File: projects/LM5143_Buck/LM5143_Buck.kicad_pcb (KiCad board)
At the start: 4 copper layers, 0 parts

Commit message: Placement
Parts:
- added C1: 4.7uF, Capacitor_SMD:C_1210_3225Metric, B.Cu at (127.8, 109.2)
- added C10: 2.2uF, Capacitor_SMD:C_0805_2012Metric, B.Cu at (144.5, 110.5)
- added C11: 10uF, Capacitor_SMD:C_1210_3225Metric, B.Cu at (124.2, 127.2)
- added C12: 100uF, Capacitor_THT:CP_Radial_D8.0mm_P3.50mm, F.Cu at (126.4, 130.2)
- added C13: 100uF, Capacitor_THT:CP_Radial_D8.0mm_P3.50mm, F.Cu at (153.6, 130.2)
- added C14: 10uF, Capacitor_SMD:C_1210_3225Metric, B.Cu at (155.8, 127.2)
- added C15: 100nF, Capacitor_SMD:C_0603_1608Metric, B.Cu at (135.0, 113.5)
- added C16: 100nF, Capacitor_SMD:C_0603_1608Metric, B.Cu at (145.0, 113.5)
- added C17: 3.3nF, Capacitor_SMD:C_0603_1608Metric, B.Cu at (145.5, 106.2)
- added C18: 82pF, Capacitor_SMD:C_0603_1608Metric, B.Cu at (145.5, 103.2)
- added C19: 100nF, Capacitor_SMD:C_0603_1608Metric, B.Cu at (145.5, 101.8)
- added C2: 4.7uF, Capacitor_SMD:C_1210_3225Metric, B.Cu at (131.2, 109.2)
- added C20: 470nF, Capacitor_SMD:C_0603_1608Metric, B.Cu at (137.5, 100.0)
- added C21: 470nF, Capacitor_SMD:C_0603_1608Metric, B.Cu at (139.2, 100.0)
- added C22: 10nF, Capacitor_SMD:C_0603_1608Metric, B.Cu at (142.8, 100.0)
- added C23: 1uF, Capacitor_SMD:C_0603_1608Metric, B.Cu at (150.8, 98.8)
- added C24: 1uF, Capacitor_SMD:C_0603_1608Metric, B.Cu at (144.8, 98.8)
- added C25: 100nF, Capacitor_SMD:C_0603_1608Metric, B.Cu at (130.2, 94.8)
- added C26: 1uF, Capacitor_SMD:C_0603_1608Metric, B.Cu at (132.8, 98.8)
- added C3: 4.7uF, Capacitor_SMD:C_1210_3225Metric, B.Cu at (148.8, 109.2)
- added C4: 4.7uF, Capacitor_SMD:C_1210_3225Metric, B.Cu at (152.2, 109.2)
- added C5: 330uF, Capacitor_THT:CP_Radial_D12.5mm_P5.00mm, F.Cu at (127.5, 89.8)
- added C6: 330uF, Capacitor_THT:CP_Radial_D12.5mm_P5.00mm, F.Cu at (141.0, 89.8)
- added C7: 330uF, Capacitor_THT:CP_Radial_D12.5mm_P5.00mm, F.Cu at (154.5, 89.8)
- added C8: 330uF, Capacitor_THT:CP_Radial_D12.5mm_P5.00mm, F.Cu at (168.0, 89.8)
- added C9: 2.2uF, Capacitor_SMD:C_0805_2012Metric, B.Cu at (135.5, 110.5)
- added D1: V2PM10L, Diode_SMD:D_SMP_DO-220AA, B.Cu at (138.2, 111.8)
- added D10: PLZ5V1C, footprints:D_MicroSMF, F.Cu at (137.8, 114.2)
- added D11: CUS10S30, Diode_SMD:D_SOD-323_HandSoldering, F.Cu at (147.0, 114.2)
- added D12: PLZ5V1C, footprints:D_MicroSMF, F.Cu at (142.2, 114.2)
- added D13: B18W1NG--20C000114U1930, LED_SMD:LED_0603_1608Metric, B.Cu at (134.5, 104.8)
- added D2: V2PM10L, Diode_SMD:D_SMP_DO-220AA, B.Cu at (141.8, 111.8)
- added D3: CUS10S30, Diode_SMD:D_SOD-323_HandSoldering, F.Cu at (133.0, 109.8)
- added D4: PLZ5V1C, footprints:D_MicroSMF, F.Cu at (137.8, 109.8)
- added D5: CUS10S30, Diode_SMD:D_SOD-323_HandSoldering, F.Cu at (147.0, 109.8)
- added D6: PLZ5V1C, footprints:D_MicroSMF, F.Cu at (142.2, 109.8)
- added D7: MBR15H120PC-AU, Package_TO_SOT_SMD:TO-277A, B.Cu at (129.8, 114.2)
- added D8: MBR15H120PC-AU, Package_TO_SOT_SMD:TO-277A, B.Cu at (150.2, 114.2)
- added D9: CUS10S30, Diode_SMD:D_SOD-323_HandSoldering, F.Cu at (133.0, 114.2)
- added J1: Bat In, footprints:XT60PW-F, F.Cu at (111.0, 84.5)
- added J2: 24V Out, footprints:XT60PW-F, F.Cu at (140.0, 135.5)
- added J3: I2C Socket, Connector_JST:JST_GH_SM04B-GHS-TB_1x04-1MP_P1.25mm_Horizontal, F.Cu at (178.2, 98.5)
- added J4: I2C Socket, Connector_JST:JST_GH_SM04B-GHS-TB_1x04-1MP_P1.25mm_Horizontal, F.Cu at (101.8, 98.5)
- added L1: 10uH, footprints:ER26A, F.Cu at (98.2, 117.5)
- added L2: 10uH, footprints:ER26A, F.Cu at (181.8, 117.5)
- added NT1: NetTie_2, footprints:NetTie-2_SMD_Pad0.25mm, B.Cu at (139.8, 103.2)
- added Q1: IGC025S08S1, footprints:PG‑TSON‑6, F.Cu at (129.2, 109.8)
- added Q2: IGC025S08S1, footprints:PG‑TSON‑6, F.Cu at (150.8, 109.8)
- added Q3: IGC025S08S1, footprints:PG‑TSON‑6, F.Cu at (129.2, 114.2)
- added Q4: IGC025S08S1, footprints:PG‑TSON‑6, F.Cu at (150.8, 114.2)
- added R1: 2.2, Resistor_SMD:R_0603_1608Metric, B.Cu at (136.2, 115.2)
- added R10: 2.2m, footprints:ASR2512, B.Cu at (151.0, 124.8)
- added R11: 3.3, Resistor_SMD:R_0603_1608Metric, F.Cu at (136.2, 114.5)
- added R12: 3.3, Resistor_SMD:R_0603_1608Metric, F.Cu at (143.8, 114.5)
- added R13: 10k, Resistor_SMD:R_0603_1608Metric, F.Cu at (139.2, 114.5)
- added R14: 10k, Resistor_SMD:R_0603_1608Metric, F.Cu at (140.8, 114.5)
- added R15: 1, Resistor_SMD:R_0603_1608Metric, F.Cu at (134.8, 114.5)
- added R16: 1, Resistor_SMD:R_0603_1608Metric, F.Cu at (145.2, 114.5)
- added R17: 3.3k, Resistor_SMD:R_0603_1608Metric, B.Cu at (134.5, 106.2)
- added R18: 100k, Resistor_SMD:R_0603_1608Metric, B.Cu at (141.0, 100.0)
- added R19: 18k, Resistor_SMD:R_0603_1608Metric, B.Cu at (145.5, 104.8)
- added R2: 2.2, Resistor_SMD:R_0603_1608Metric, B.Cu at (143.8, 115.2)
- added R20: 10k, Resistor_SMD:R_0603_1608Metric, B.Cu at (152.5, 98.8)
- added R21: 390k, Resistor_SMD:R_0603_1608Metric, B.Cu at (134.5, 101.8)
- added R22: 10k, Resistor_SMD:R_0603_1608Metric, B.Cu at (134.5, 103.2)
- added R23: 3.3k, Resistor_SMD:R_0603_1608Metric, B.Cu at (123.5, 97.0)
- added R24: 3.3k, Resistor_SMD:R_0603_1608Metric, B.Cu at (123.5, 95.2)
- added R25: 3.3k, Resistor_SMD:R_0603_1608Metric, B.Cu at (127.0, 94.8)
- added R26: 10, Resistor_SMD:R_0603_1608Metric, B.Cu at (130.2, 100.2)
- added R27, R30: 5m, footprints:PCSR2512_Alt, B.Cu at (140.0, 123.2)
- added R28: 5m, footprints:PCSR2512_Alt_2, B.Cu at (148.0, 123.2)
- added R29: 5m, footprints:PCSR2512_Alt_2, B.Cu at (144.0, 123.2)
- added R3: 3.3, Resistor_SMD:R_0603_1608Metric, F.Cu at (136.2, 109.5)
- added R31: 10, Resistor_SMD:R_0603_1608Metric, B.Cu at (134.5, 98.8)
- added R4: 3.3, Resistor_SMD:R_0603_1608Metric, F.Cu at (143.8, 109.5)
- added R5: 10k, Resistor_SMD:R_0603_1608Metric, F.Cu at (139.2, 109.5)
- added R6: 10k, Resistor_SMD:R_0603_1608Metric, F.Cu at (140.8, 109.5)
- added R7: 1, Resistor_SMD:R_0603_1608Metric, F.Cu at (134.8, 109.5)
- added R8: 1, Resistor_SMD:R_0603_1608Metric, F.Cu at (145.2, 109.5)
- added R9: 2.2m, footprints:ASR2512, B.Cu at (129.0, 124.8)
- added SW1: Addr_Switch, footprints:SLW-1478144-5A-S-D, F.Cu at (115.5, 99.0)
- added SW2: Addr_Switch, footprints:SLW-1478144-5A-S-D, F.Cu at (164.5, 99.0)
- added TP1: TestPoint, TestPoint:TestPoint_Keystone_5000-5004_Miniature, F.Cu at (100.8, 90.5)
- added TP2: TestPoint, TestPoint:TestPoint_Keystone_5000-5004_Miniature, F.Cu at (121.2, 90.5)
- added TP3: TestPoint, TestPoint:TestPoint_Keystone_5000-5004_Miniature, F.Cu at (123.8, 107.0)
- added TP4: TestPoint, TestPoint:TestPoint_Keystone_5000-5004_Miniature, F.Cu at (156.2, 106.8)
- added TP5: TestPoint, TestPoint:TestPoint_Keystone_5000-5004_Miniature, F.Cu at (150.2, 135.5)
- added TP6: TestPoint, TestPoint:TestPoint_Keystone_5000-5004_Miniature, F.Cu at (129.8, 135.5)
- added TP7: TestPoint, TestPoint:TestPoint_Pad_D2.0mm, B.Cu at (118.0, 96.0)
- added U1: ~, footprints:Texas_VQFN-40-1EP_6x6mm_P0.5mm_EP3.3x3.3mm_ThermalVias, B.Cu at (140.0, 105.5)
- added U2: TLV74033, Package_TO_SOT_SMD:SOT-23-5, B.Cu at (147.8, 98.8)
- added U3: INA226, Package_SO:VSSOP-10_3x3mm_P0.5mm, B.Cu at (128.5, 97.5)
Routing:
- net VOUT: track 0.00 -> 37.3 mm
- net +24V: track 0.00 -> 11.2 mm, vias 0 -> 55
- net PGND1: track 0.00 -> 8.78 mm
- net PGND2: track 0.00 -> 8.61 mm
- net Net-(D3-A): track 0.00 -> 8.61 mm
- net Net-(D3-K): track 0.00 -> 8.61 mm
- net Net-(D11-K): track 0.00 -> 8.61 mm
- net Net-(D5-A): track 0.00 -> 8.41 mm
- net Net-(D10-K): track 0.00 -> 7.99 mm
- net Net-(D5-K): track 0.00 -> 7.99 mm
- net Net-(U1-CS1): track 0.00 -> 4.98 mm
- net Net-(U1-CS2): track 0.00 -> 4.98 mm
- added copper zone on B.Cu, net +24V
- added copper zone on F.Cu, net +24V
- added copper zone on B.Cu, net GNDA
- added copper zone on B.Cu, net GNDPWR
- added copper zone on F.Cu, net GNDPWR
- added copper zone on In1.Cu, net GNDPWR
- added copper zone on In2.Cu, net GNDPWR
- added copper zone on B.Cu, net Net-(D7-K)
- added copper zone on F.Cu, net Net-(D7-K)
- added copper zone on B.Cu, net Net-(D8-K)
- added copper zone on F.Cu, net Net-(D8-K)
- added copper zone on B.Cu, net VDD
- added copper zone on F.Cu, net VDD
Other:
- board outline added: 83 x 55 mm
- board text added: "Heat Sink Area"

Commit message: PCB wiring
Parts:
- C17, R17, R19: moved to F.Cu
- moved SW2 49.1 mm to (164.5, 102.0), turned to 180 degrees
- moved SW1 49.0 mm to (115.5, 99.0)
- moved R19 3.01 mm to (145.8, 101.8)
- moved C17 2.24 mm to (146.5, 104.2), turned to 90 degrees
- moved D13 1.27 mm to (134.2, 106.0)
- moved R1 0.83 mm to (136.6, 116.0)
- moved R2 0.83 mm to (143.4, 116.0)
- moved D1 0.80 mm to (138.2, 112.6)
- moved D2 0.80 mm to (141.8, 112.6)
- moved D10 0.50 mm to (137.8, 114.8)
- moved D11 0.50 mm to (147.0, 114.8)
- moved D12 0.50 mm to (142.2, 114.8)
- moved D7 0.50 mm to (129.8, 114.8)
- moved D8 0.50 mm to (150.2, 114.8)
- moved D9 0.50 mm to (133.0, 114.8)
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- renumbered SW2 to SW1, SW1 to SW2
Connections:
- J1 pad : VDD -> GNDPWR
- J2 pad : +24V -> GNDPWR
- SW1 pad : VDD -> GNDPWR
- SW2 pad : VDD -> GNDPWR
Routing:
- net Net-(J3-Pin_3): track 0.00 -> 83.4 mm, vias 0 -> 1
- net Net-(J3-Pin_4): track 0.00 -> 82.8 mm, vias 0 -> 1
- net VOUT: track 37.3 -> 106.0 mm, vias 0 -> 6
- net +3.3V: track 0.00 -> 68.0 mm, vias 0 -> 2
- net +5V: track 0.00 -> 49.8 mm, vias 0 -> 3
- net +24V: track 11.2 -> 57.0 mm, vias 55 -> 57
- net GNDA: track 0.00 -> 45.2 mm, vias 0 -> 1
- net Net-(U3-A1): track 0.00 -> 40.0 mm, vias 0 -> 1
- net /~{Alert}: track 0.00 -> 34.9 mm, vias 0 -> 3
- net Net-(U1-CS1): track 4.98 -> 34.4 mm, vias 0 -> 2
- net Net-(U1-CS2): track 4.98 -> 33.7 mm, vias 0 -> 2
- net Net-(U1-COMP1): track 0.00 -> 15.9 mm, vias 0 -> 2
- net PGND2: track 8.61 -> 22.9 mm, vias 0 -> 2
- net Net-(U3-A0): track 0.00 -> 12.8 mm
- net Net-(U1-SS1): track 0.00 -> 11.4 mm, vias 0 -> 2
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- added copper zone on B.Cu, net VOUT

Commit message: Update stuff
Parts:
- removed the TP3 at (124.0, 107.0)
- removed the TP4 at (156.0, 107.0)
- moved J3 77.2 mm to (101.8, 88.0), turned to -90 degrees
- moved TP1 61.6 mm to (162.2, 86.8)
- moved J1 61.2 mm to (172.2, 84.5)
- moved TP2 58.3 mm to (179.2, 96.5)
- moved C5 16.2 mm to (111.2, 89.8)
- moved C6 16.2 mm to (124.8, 89.8)
- moved C7 16.2 mm to (138.2, 89.8)
- moved C8 16.2 mm to (151.8, 89.8)
- moved SW1 2.60 mm to (118.1, 99.0)
- moved SW2 2.60 mm to (161.9, 102.0)
- moved TP7 2.46 mm to (120.2, 97.0)
- renumbered TP5 to TP3, TP6 to TP4
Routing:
- net GNDA: track 45.2 -> 54.7 mm
- net +3.3V: track 68.0 -> 60.8 mm
- net Net-(J3-Pin_4): track 82.8 -> 78.1 mm, vias 1 -> 3
- net /~{Alert}: track 34.9 -> 32.3 mm
- net Net-(U3-A1): track 40.0 -> 37.4 mm
- net Net-(U3-A0): track 12.8 -> 10.2 mm
- net Net-(J3-Pin_3): track 83.4 -> 81.4 mm, vias 1 -> 3
- net VOUT: track 106.0 -> 103.9 mm
- net Net-(U1-CS1): track 34.4 -> 33.1 mm
- net Net-(U1-CS2): track 33.7 -> 32.9 mm
- net VDD: vias 21 -> 25
- net Net-(D8-K): vias 0 -> 10
- net Net-(D7-K): vias 0 -> 10
- net GNDPWR: vias 25 -> 175
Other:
- board text added: "+"
- board text added: "-"
- board text added: "24V"
- board text added: "BAT"
- board text added: "GND"
- board text added: "~{Alert}"

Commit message: minor fixes
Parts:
- moved TP1 2.25 mm to (162.2, 84.5)
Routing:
- net GNDPWR: vias 175 -> 176
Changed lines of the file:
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@@
 	(footprint "TestPoint:TestPoint_Keystone_5000-5004_Miniature"
 		(layer "F.Cu")
-		(at 162.25 86.75)
+		(at 162.25 84.5)
 		(descr "Keystone THM Miniature Test Point 5000-5004, http://www.keyelco.com/product-pdf.cfm?p=1309")
 		(tags "Through Hole Mount Test Points")
@@
 	)
 	(gr_text "BAT"
-		(at 162.25 84.25 0)
+		(at 159.25 83.75 0)
 		(layer "F.SilkS")
 		(effects
@@
 	)
 	(via
+		(at 162.5 87)
+		(size 0.6)
+		(drill 0.3)
+		(layers "F.Cu" "B.Cu")
+		(free yes)
+		(net 2)
+	)
+	(via
 		(at 162.5 114)
 		(size 0.6)
@@
 		(members "5062c024-5f6c-47a1-bfe0-1b14b4ad3ff2" "55c91df1-3d0a-4434-9000-f0a3faa70d4e")
 	)
-	(group ""
-		(members "0003389f-96c1-440a-82e1-2d7b16629ee7" "c15c7f08-a1d3-4b3f-ac85-2828c58cd0ea")
-	)
 	(embedded_fonts no)

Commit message: Minor changes
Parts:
- moved C17 1.25 mm to (145.8, 103.2), turned to 0 degrees
- renumbered TP7 to TP5
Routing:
- net GNDA: track 54.7 -> 55.8 mm

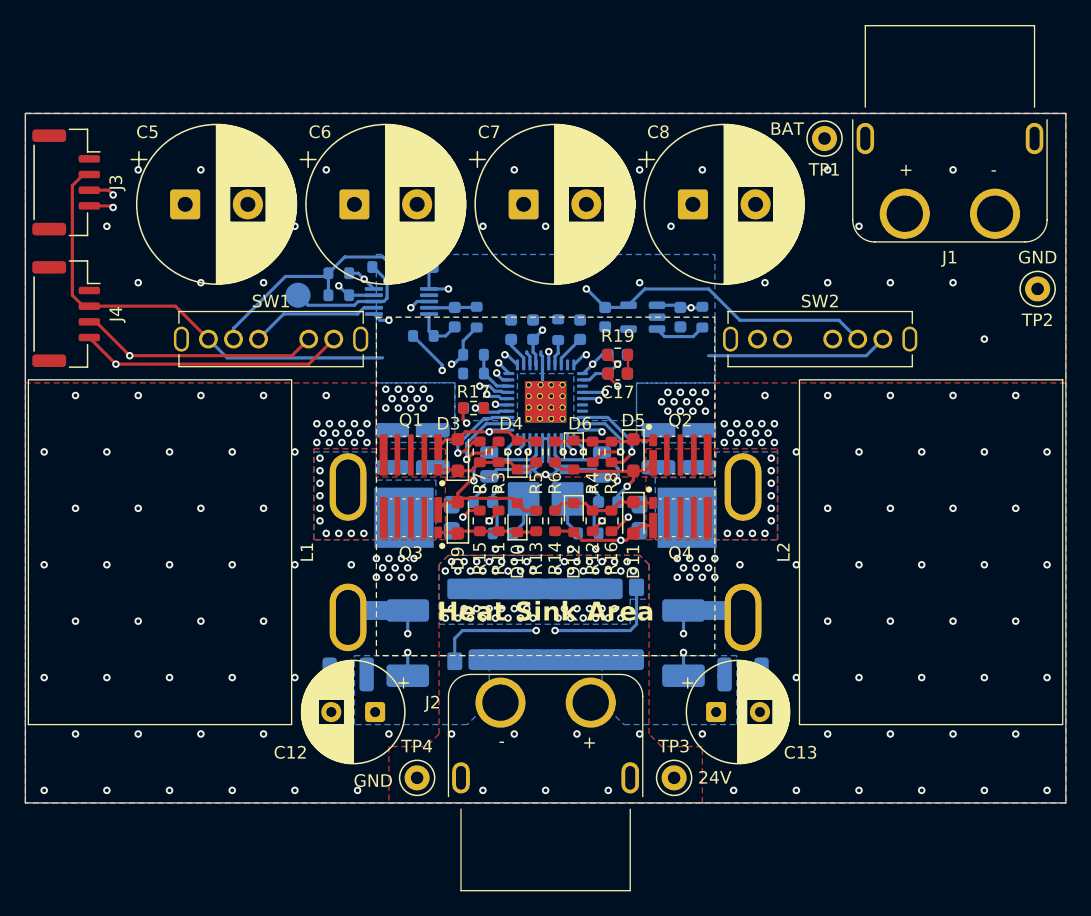
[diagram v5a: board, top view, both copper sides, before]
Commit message: Changed a few pad sizes
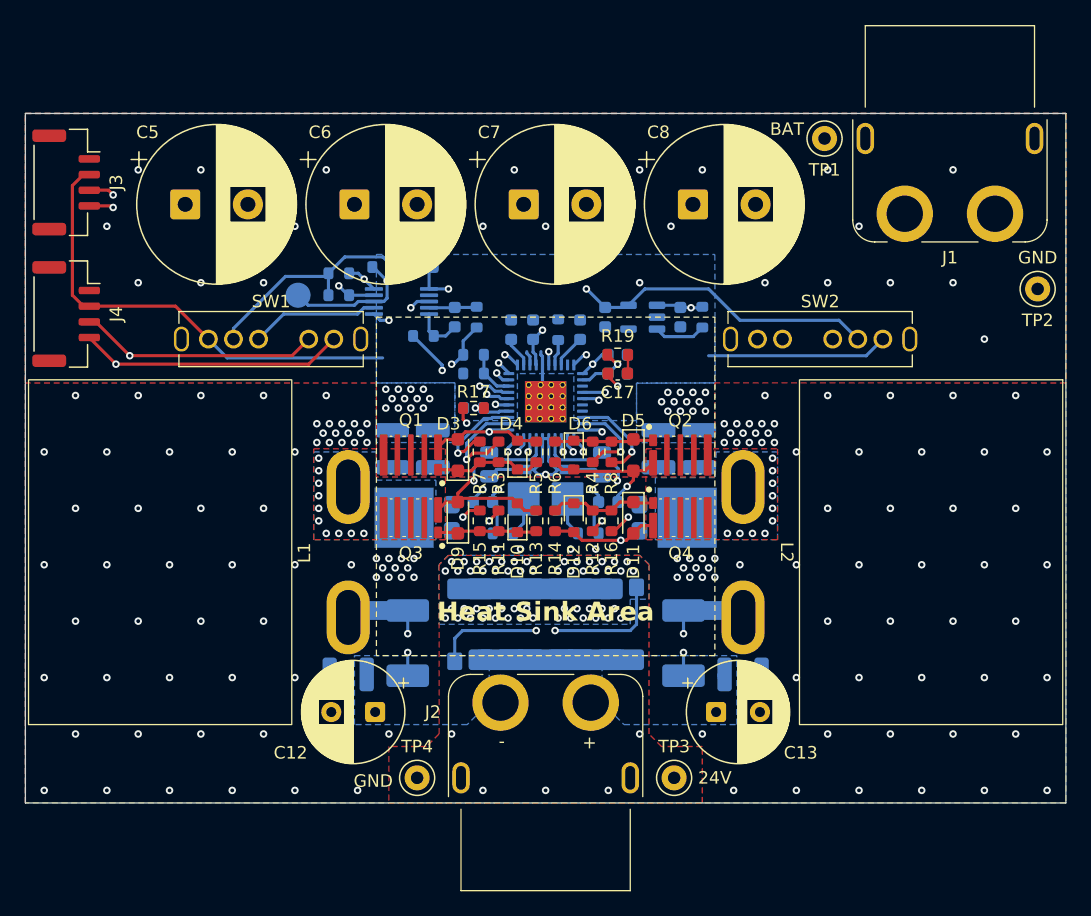
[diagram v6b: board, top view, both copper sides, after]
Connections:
- J3 pad MP: VDD -> (no net)
- J4 pad MP: VDD -> (no net)
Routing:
- net GNDPWR: vias 176 -> 174

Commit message: Change switch orientation, update XT60 name
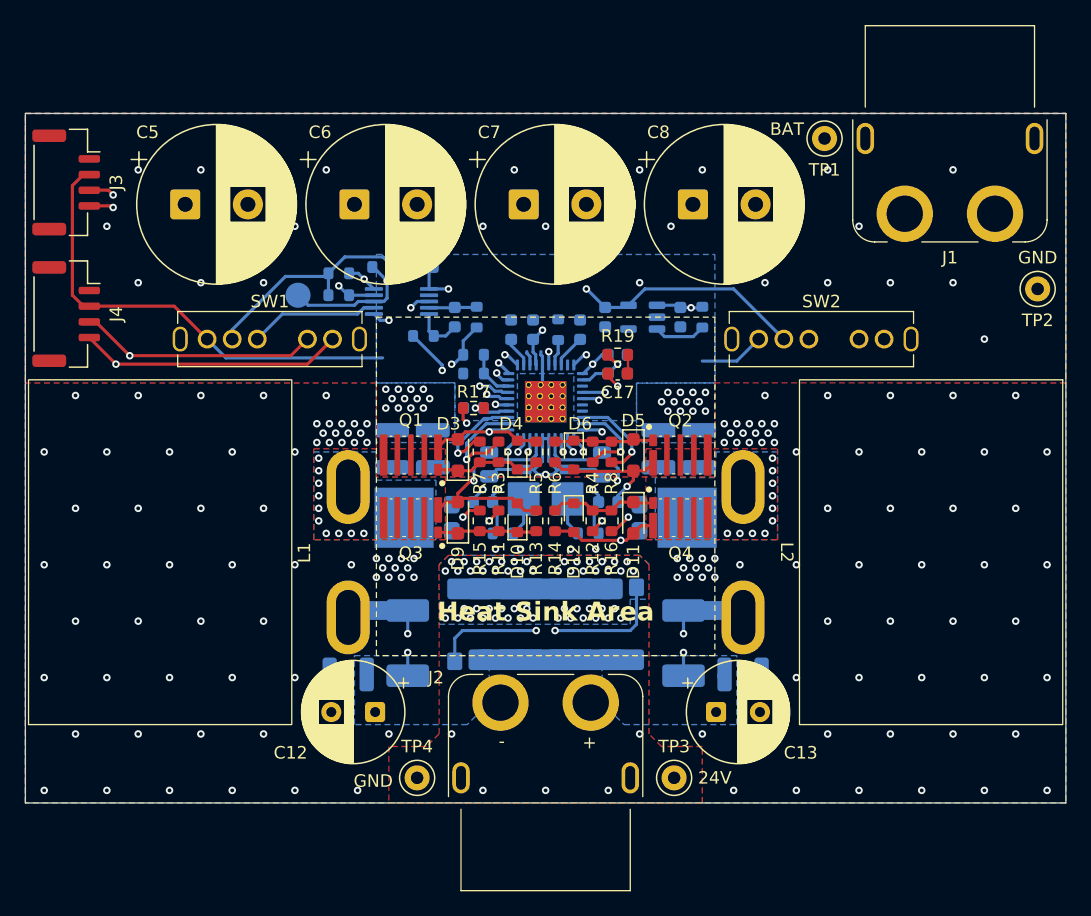
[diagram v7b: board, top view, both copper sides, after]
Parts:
- J1, J2: footprint footprints:XT60PW-F -> footprints:XT60PW
- moved SW2 3.00 mm to (162.0, 99.0), turned to 0 degrees
- moved SW1 0.10 mm to (118.0, 99.0)
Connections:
- SW1 pad : GNDPWR -> (no net)
- SW2 pad : GNDPWR -> (no net)
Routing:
- net Net-(J3-Pin_4): track 78.1 -> 88.7 mm
- net GNDA: track 55.8 -> 46.5 mm
- net Net-(J3-Pin_3): track 81.4 -> 87.4 mm
- net +3.3V: track 60.8 -> 55.0 mm
- net Net-(U3-A1): track 37.4 -> 35.5 mm

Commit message: Minor changes
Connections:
- J3 pad MP: (no net) -> VDD
- J4 pad MP: (no net) -> VDD
- SW1 pad : (no net) -> GNDPWR
- SW2 pad : (no net) -> GNDPWR
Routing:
- net GNDPWR: vias 174 -> 172
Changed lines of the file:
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@@
 			(layers "F.Cu" "F.Mask" "F.Paste")
 			(roundrect_rratio 0.25)
+			(net 1 "VDD")
 		)
 		(pad "MP" smd roundrect
@@
 			(layers "F.Cu" "F.Mask" "F.Paste")
 			(roundrect_rratio 0.25)
+			(net 1 "VDD")
 		)
 		(embedded_fonts no)
@@
 		(pad "" thru_hole oval
 			(at -7.15 1.5)
-			(size 1.2 2)
+			(size 1.4 2.2)
 			(drill oval 0.8 1.6)
 			(layers "*.Cu" "*.Mask")
 			(remove_unused_layers no)
+			(net 2 "GNDPWR")
 		)
 		(pad "" thru_hole oval
 			(at 7.15 1.5)
-			(size 1.2 2)
+			(size 1.4 2.2)
 			(drill oval 0.8 1.6)
 			(layers "*.Cu" "*.Mask")
 			(remove_unused_layers no)
+			(net 2 "GNDPWR")
 		)
 		(pad "1" thru_hole circle
@@
 			(layers "F.Cu" "F.Mask" "F.Paste")
 			(roundrect_rratio 0.25)
+			(net 1 "VDD")
 		)
 		(pad "MP" smd roundrect
@@
 			(layers "F.Cu" "F.Mask" "F.Paste")
 			(roundrect_rratio 0.25)
+			(net 1 "VDD")
 		)
 		(embedded_fonts no)
@@
 		(pad "" thru_hole oval
 			(at -7.15 1.5)
-			(size 1.2 2)
+			(size 1.4 2.2)
 			(drill oval 0.8 1.6)
 			(layers "*.Cu" "*.Mask")
 			(remove_unused_layers no)
+			(net 2 "GNDPWR")
 		)
 		(pad "" thru_hole oval
 			(at 7.15 1.5)
-			(size 1.2 2)
+			(size 1.4 2.2)
 			(drill oval 0.8 1.6)
 			(layers "*.Cu" "*.Mask")
 			(remove_unused_layers no)
+			(net 2 "GNDPWR")
 		)
 		(pad "1" thru_hole circle
@@
 		(sheetname "/")
 		(sheetfile "LM5143_Buck.kicad_sch")
+		(solder_paste_margin -0.05)
 		(attr smd)
 		(fp_line
@@
 		(sheetname "/")
 		(sheetfile "LM5143_Buck.kicad_sch")
+		(solder_paste_margin -0.05)
 		(attr smd)
 		(fp_line
@@
 	)
 	(via
-		(at 150 91.5)
-		(size 0.6)
-		(drill 0.3)
-		(layers "F.Cu" "B.Cu")
-		(free yes)
-		(net 2)
-	)
-	(via
 		(at 140 136.5)
 		(size 0.6)
@@
 		(size 0.6)
 		(drill 0.3)
-		(layers "F.Cu" "B.Cu")
-		(free yes)
-		(net 2)
-	)
-	(via
-		(at 140 91.5)
-		(size 0.6)
-		(drill 0.3)
